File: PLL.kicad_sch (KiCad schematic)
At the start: 88 parts, among them J301 Vtune, J302 RFShield_TwoPieces, J303 CPout, J304 DNP, J305 DNP, J306 DNP, J307 DNP, J308 DNP, U301 LMX2572, U302 XC6204B33

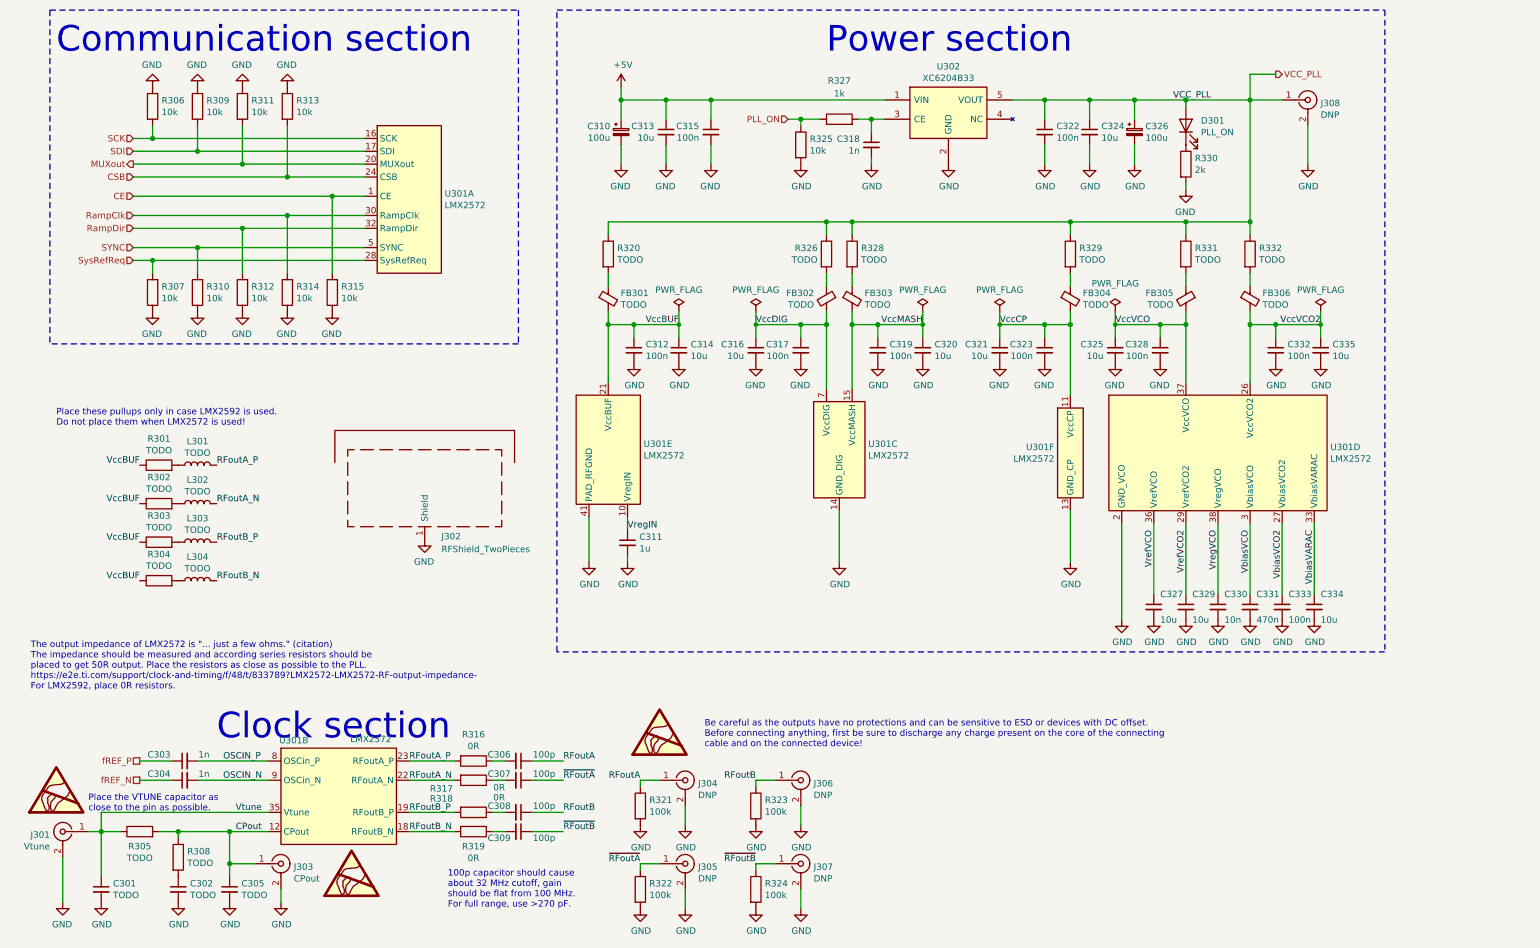
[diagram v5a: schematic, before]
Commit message: Schematic checked. All footprints assigned. Electrolytics need footprint check, so do the RS485 and power connectors and the MuRata oscillator (also it is now EOL) and the crystal. The power protection transils on aux input/output need replacement. PCB in sync with SCH.
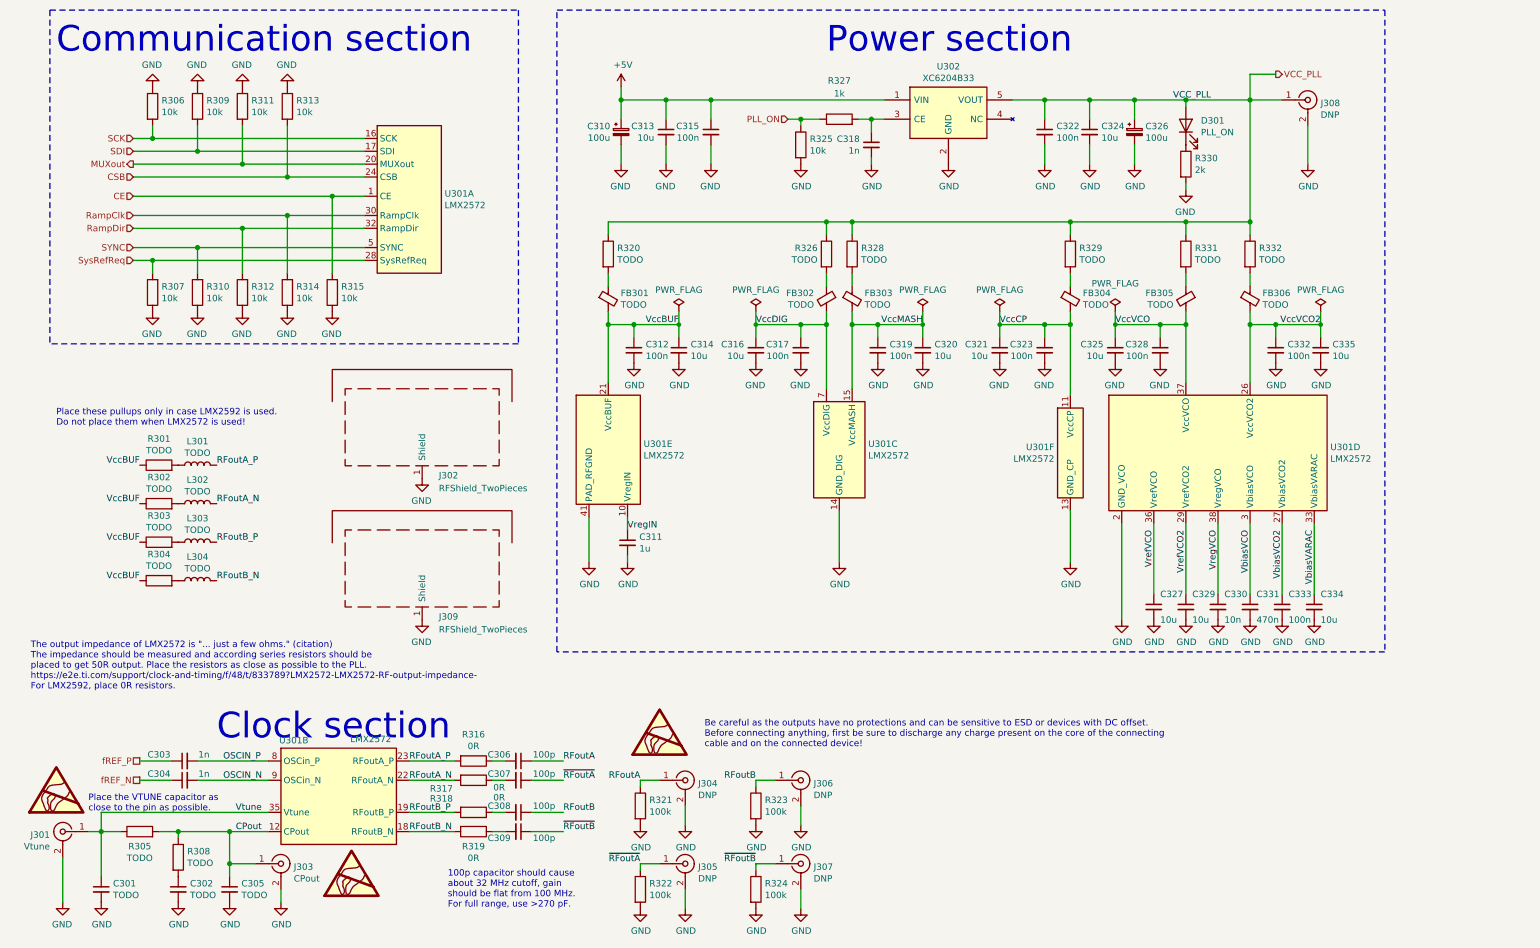
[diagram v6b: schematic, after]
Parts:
- added J309: RFShield_TwoPieces, RF_Shielding:Laird_Technologies_BMI-S-205-F_38.10x25.40mm, symbol Device:RFShield_TwoPieces
- J302: footprint RF_Shielding:Laird_Technologies_BMI-S-206-F_36.83x33.68mm -> RF_Shielding:Laird_Technologies_BMI-S-205-F_38.10x25.40mm
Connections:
- net GND: now also J309.1 (Shield)
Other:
- moved on the sheet: J302

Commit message: Resolved all broken symbols / packages / links except TCXO.
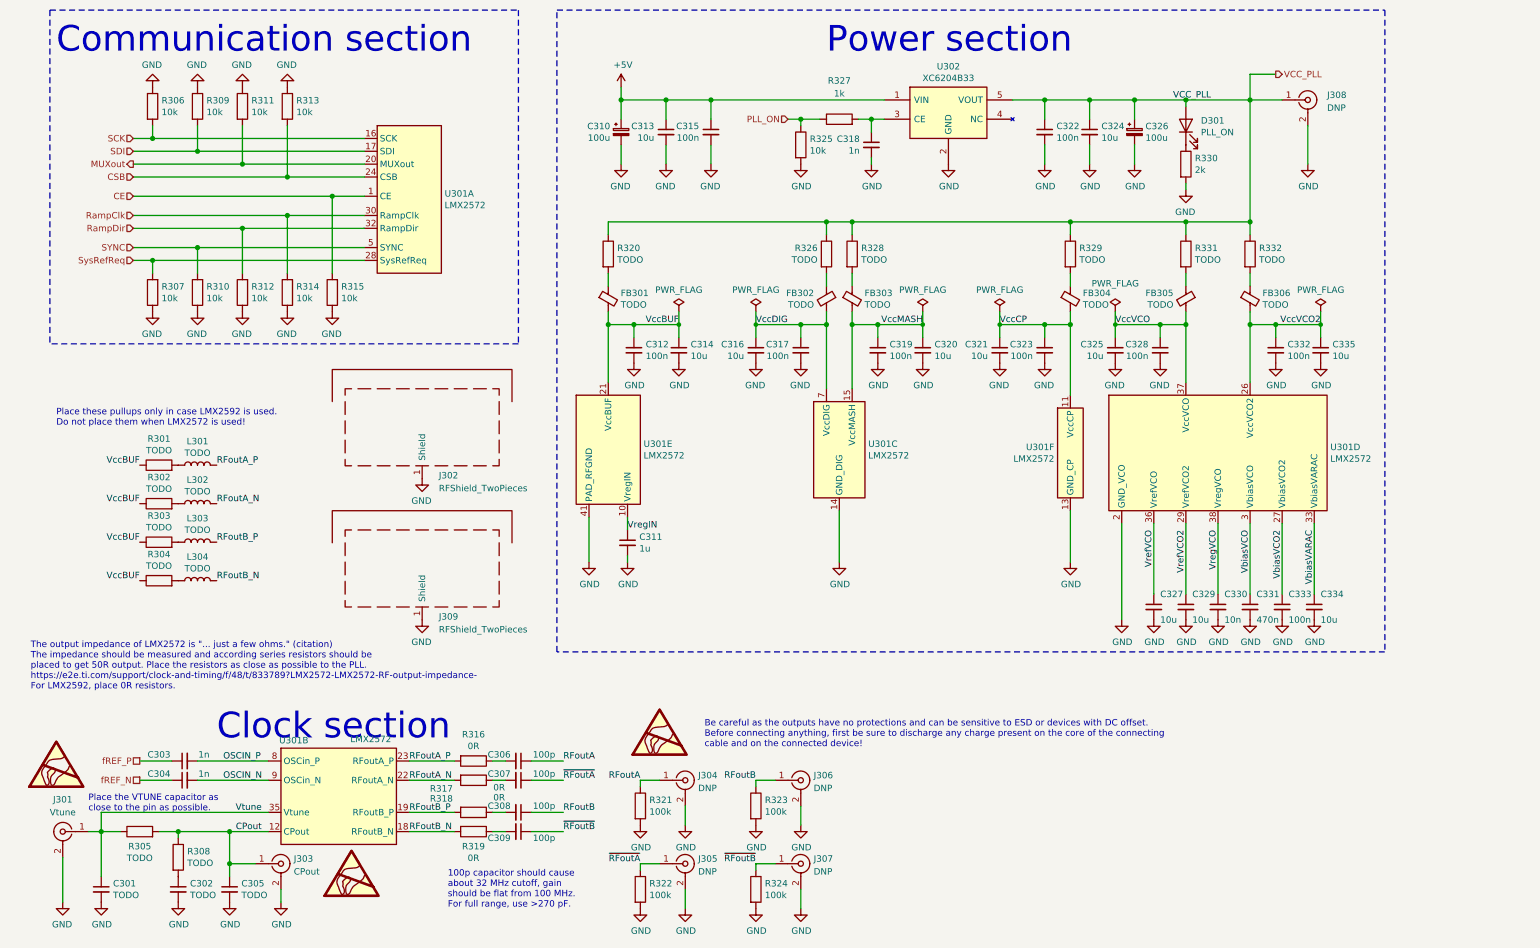
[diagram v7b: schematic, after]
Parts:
- removed J301: Vtune, Connector_Coaxial:U.FL_Molex_MCRF_73412-0110_Vertical, symbol Connector:Conn_Coaxial
- removed J303: CPout, Connector_Coaxial:U.FL_Molex_MCRF_73412-0110_Vertical, symbol Connector:Conn_Coaxial
- removed J304, J305, J306, J307: DNP, petr_kicad:SMA_rosenberger_hybrid, symbol Connector:Conn_Coaxial
- removed J308: DNP, Connector_Coaxial:U.FL_Molex_MCRF_73412-0110_Vertical, symbol Connector:Conn_Coaxial
- added J301: Vtune, Connector_Coaxial:U.FL_Molex_MCRF_73412-0110_Vertical, symbol petr:u.FL
- added J303: CPout, Connector_Coaxial:U.FL_Molex_MCRF_73412-0110_Vertical, symbol petr:u.FL
- added J304, J305, J306, J307: DNP, petr_kicad:SMA_rosenberger_hybrid, symbol petr:SMA_Rosenberger_32K243-40ML5_chinese_SMA_hybrid
- added J308: DNP, Connector_Coaxial:U.FL_Molex_MCRF_73412-0110_Vertical, symbol petr:u.FL
- U301: symbol petr_lib_nightly:LMX2572 -> petr:LMX2572
- U302: symbol petr_lib_nightly:XC6204B33 -> petr:XC6204B33
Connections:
- net CPout: now also J303.1 (In)
- net GND: now also J301.2 (Ext), J303.2 (Ext), J304.2 (Ext), J305.2 (Ext), J306.2 (Ext), J307.2 (Ext), J308.2 (Ext)
- net RFoutA: now also J304.1 (In)
- net RFoutB: now also J306.1 (In)
- net VCC_PLL: now also J308.1 (In)
- net Vtune: now also J301.1 (In)
- net ~{RFoutA}: now also J305.1 (In)
- net ~{RFoutB}: now also J307.1 (In)

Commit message: Footprint changes
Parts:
- C310, C326: footprint Capacitor_SMD:CP_Elec_6.3x7.7 -> Capacitor_SMD:CP_Elec_6.3x5.8; symbol Device:C_Polarized_Small -> petr:CP_47uF_35V
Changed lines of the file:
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@@
     (pin "2")
   )
-  (symbol (lib_id "Device:C_Polarized_Small") (at 132.08 38.1 0) (unit 1)
+  (symbol (lib_id "petr:CP_47uF_35V") (at 132.08 38.1 0) (unit 1)
     (in_bom yes) (on_board yes)
     (property "Reference" "C310" (id 0) (at 129.9209 36.9506 0)
@@
       (effects (font (size 1.27 1.27)) (justify right))
     )
-    (property "Footprint" "Capacitor_SMD:CP_Elec_6.3x7.7" (id 2) (at 132.08 38.1 0)
-      (effects (font (size 1.27 1.27)) hide)
-    )
-    (property "Datasheet" "~" (id 3) (at 132.08 38.1 0)
+    (property "Footprint" "Capacitor_SMD:CP_Elec_6.3x5.8" (id 2) (at 132.08 38.1 0)
+      (effects (font (size 1.27 1.27)) hide)
+    )
+    (property "Datasheet" "http://www.samwha.com/electric/product/list_pdf2/CK.pdf" (id 3) (at 132.08 38.1 0)
       (effects (font (size 1.27 1.27)) hide)
     )
@@
     (pin "2")
   )
-  (symbol (lib_id "Device:C_Polarized_Small") (at 233.68 38.1 0) (unit 1)
+  (symbol (lib_id "petr:CP_47uF_35V") (at 233.68 38.1 0) (unit 1)
     (in_bom yes) (on_board yes)
     (property "Reference" "C326" (id 0) (at 235.8391 36.9506 0)
@@
       (effects (font (size 1.27 1.27)) (justify left))
     )
-    (property "Footprint" "Capacitor_SMD:CP_Elec_6.3x7.7" (id 2) (at 233.68 38.1 0)
-      (effects (font (size 1.27 1.27)) hide)
-    )
-    (property "Datasheet" "~" (id 3) (at 233.68 38.1 0)
-      (effects (font (size 1.27 1.27)) hide)
-    )
+    (property "Footprint" "Capacitor_SMD:CP_Elec_6.3x5.8" (id 2) (at 233.68 38.1 0)
+      (effects (font (size 1.27 1.27)) hide)
+    )
+    (property "Datasheet" "http://www.samwha.com/electric/product/list_pdf2/CK.pdf" (id 3) (at 233.68 38.1 0)
+      (effects (font (size 1.27 1.27)) hide)
+    )
